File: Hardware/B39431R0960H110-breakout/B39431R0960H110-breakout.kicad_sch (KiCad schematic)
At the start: 4 parts, among them J1 Conn_Coaxial_x2, U1 RF1404D

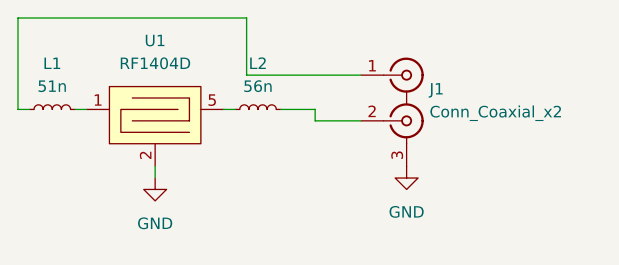
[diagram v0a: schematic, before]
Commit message: SAW Breakout: DRC ERC Pass
Ready for PR
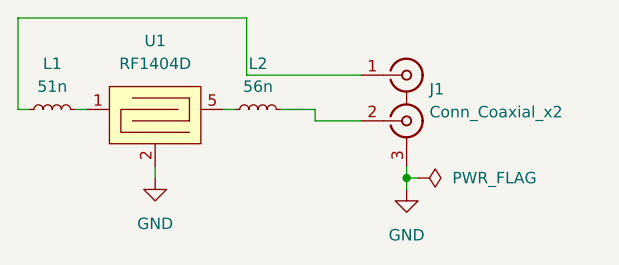
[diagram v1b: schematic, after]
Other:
- company: (none) -> GQC
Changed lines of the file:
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@@
     (title "SAW Filter Breakout")
     (date "2022-07-01")
+    (company "GQC")
+    (comment 1 "Designed by Hans Gaensbauer")
+  )
+  (junction (at 168.91 107.95) (diameter 0) (color 0 0 0 0)
   )
   (wire (pts (xy 151.13 90.17) (xy 125.73 90.17))
@@
   )
   (wire (pts (xy 140.97 106.68) (xy 140.97 107.95))
+    (stroke (width 0) (type default) (color 0 0 0 0))
+  )
+  (wire (pts (xy 168.91 107.95) (xy 170.18 107.95))
+    (stroke (width 0) (type default) (color 0 0 0 0))
+  )
+  (wire (pts (xy 168.91 109.22) (xy 168.91 107.95))
+    (stroke (width 0) (type default) (color 0 0 0 0))
+  )
+  (wire (pts (xy 168.91 107.95) (xy 168.91 106.68))
     (stroke (width 0) (type default) (color 0 0 0 0))
   )
@@
     (pin "1")
   )
-  (symbol (lib_id "power:GND") (at 168.91 106.68 0) (unit 1)
+  (symbol (lib_id "power:PWR_FLAG") (at 170.18 107.95 270) (unit 1)
     (in_bom yes) (on_board yes) (fields_autoplaced)
-    (property "Reference" "#PWR02" (id 0) (at 168.91 113.03 0)
+    (property "Reference" "#FLG0101" (id 0) (at 172.085 107.95 0)
       (effects (font (size 1.27 1.27)) hide)
     )
-    (property "Value" "GND" (id 1) (at 168.91 111.76 0))
-    (property "Footprint" "" (id 2) (at 168.91 106.68 0)
+    (property "Value" "PWR_FLAG" (id 1) (at 173.99 107.9499 90)
+      (effects (font (size 1.27 1.27)) (justify left))
+    )
+    (property "Footprint" "" (id 2) (at 170.18 107.95 0)
       (effects (font (size 1.27 1.27)) hide)
     )
-    (property "Datasheet" "" (id 3) (at 168.91 106.68 0)
+    (property "Datasheet" "~" (id 3) (at 170.18 107.95 0)
+      (effects (font (size 1.27 1.27)) hide)
+    )
+    (pin "1")
+  )
+  (symbol (lib_id "power:GND") (at 168.91 109.22 0) (unit 1)
+    (in_bom yes) (on_board yes) (fields_autoplaced)
+    (property "Reference" "#PWR02" (id 0) (at 168.91 115.57 0)
+      (effects (font (size 1.27 1.27)) hide)
+    )
+    (property "Value" "GND" (id 1) (at 168.91 114.3 0))
+    (property "Footprint" "" (id 2) (at 168.91 109.22 0)
+      (effects (font (size 1.27 1.27)) hide)
+    )
+    (property "Datasheet" "" (id 3) (at 168.91 109.22 0)
       (effects (font (size 1.27 1.27)) hide)
     )
@@
   )
   (symbol_instances
+    (path "/42eb9c28-7f4b-4f81-bf35-4b5320a6e00b"
+      (reference "#FLG0101") (unit 1) (value "PWR_FLAG") (footprint "")
+    )
     (path "/1e89d3ea-13eb-4302-b473-aa5d55a87135"
       (reference "#PWR01") (unit 1) (value "GND") (footprint "")
